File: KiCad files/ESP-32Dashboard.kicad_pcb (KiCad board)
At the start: 2 copper layers, 43.9 x 47 mm, 5 parts, among them J1 Conn_01x08_Pin, J4 JST-BEC, U1 XIAO-ESP32-S3-SMD

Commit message: Small changes to the pcb + new renders
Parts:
- moved J4 6.72 mm to (95.5, 98.6), turned to 0 degrees
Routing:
- net Net-(J4-Pin_1): track 63.3 -> 56.4 mm
- net GND: track 73.7 -> 76.5 mm

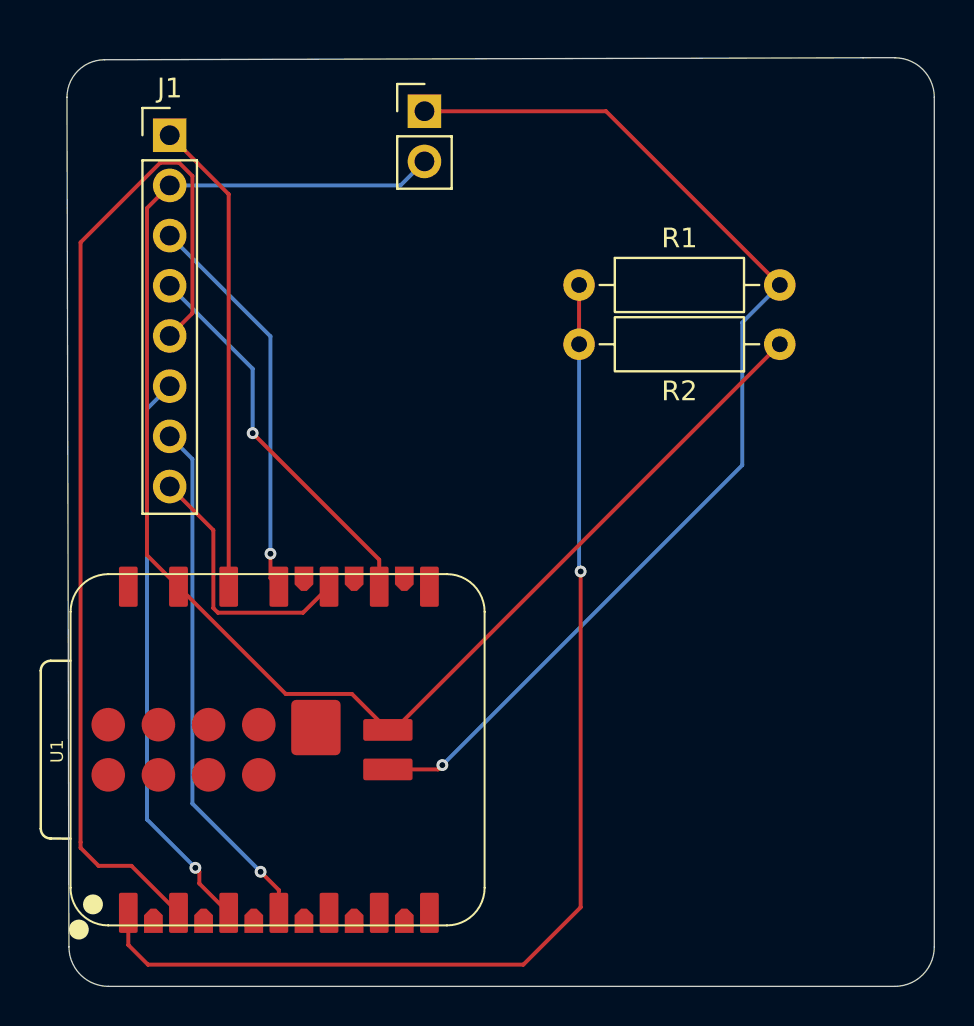
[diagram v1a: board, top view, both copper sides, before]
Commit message: fixed edge.cuts
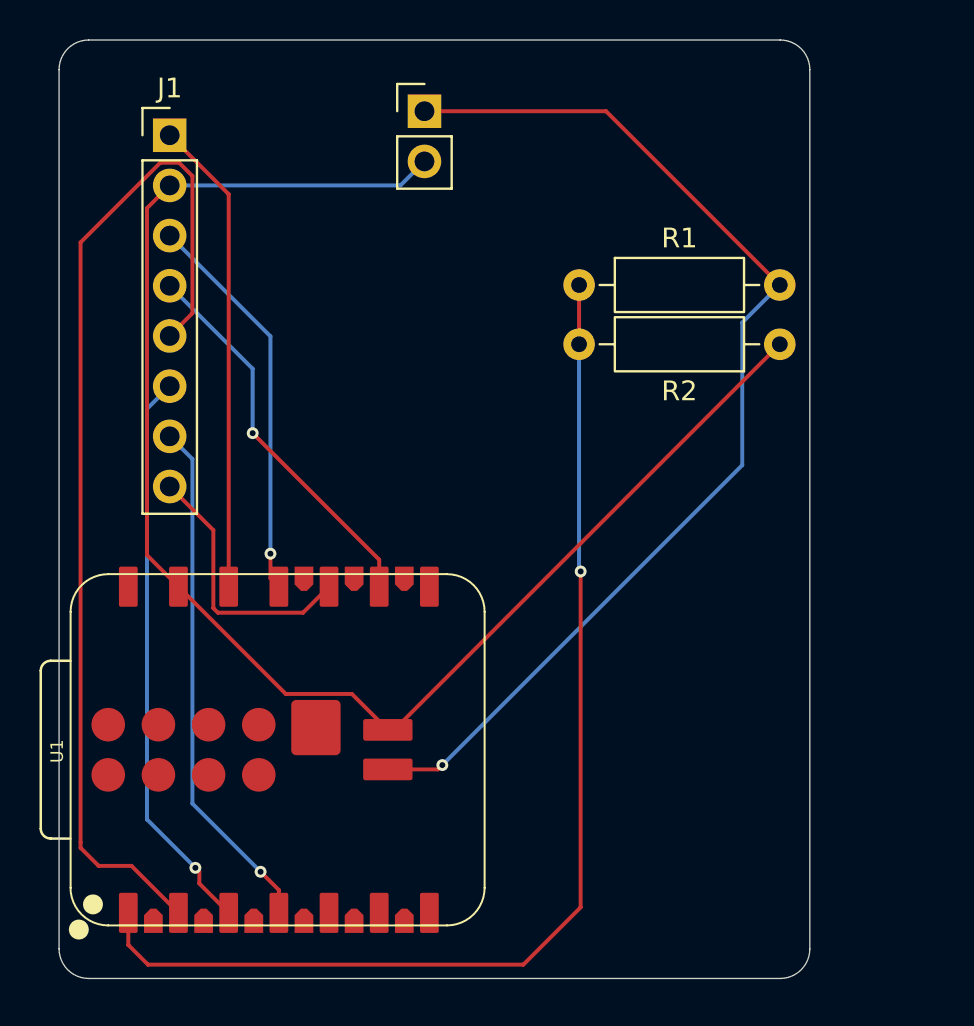
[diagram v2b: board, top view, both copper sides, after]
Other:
- board size 43.9 x 47 mm -> 38 x 47.5 mm
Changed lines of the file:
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@@
 	)
 	(gr_arc
-		(start 77.4 97.9)
-		(mid 77.956497 96.556497)
-		(end 79.3 96)
+		(start 77 96.5)
+		(mid 77.43934 95.43934)
+		(end 78.5 95)
 		(stroke
 			(width 0.05)
@@
 	)
 	(gr_line
-		(start 77.5 140.9)
-		(end 77.4 97.9)
+		(start 77 141)
+		(end 77 96.5)
 		(stroke
 			(width 0.05)
@@
 	)
 	(gr_line
-		(start 79.3 96)
-		(end 117.7 95.9)
+		(start 78.5 95)
+		(end 113.5 95)
 		(stroke
 			(width 0.05)
@@
 	)
 	(gr_arc
-		(start 79.5 142.9)
-		(mid 78.085786 142.314214)
-		(end 77.5 140.9)
+		(start 78.5 142.5)
+		(mid 77.43934 142.06066)
+		(end 77 141)
+		(stroke
+			(width 0.05)
+			(type default)
+		)
+		(layer "Edge.Cuts")
+	)
+	(gr_arc
+		(start 113.5 95)
+		(mid 114.56066 95.43934)
+		(end 115 96.5)
 		(stroke
 			(width 0.05)
@@
 	)
 	(gr_line
-		(start 117.7 95.9)
-		(end 119.3 95.895833)
+		(start 113.5 142.5)
+		(end 78.5 142.5)
+		(stroke
+			(width 0.05)
+			(type default)
+		)
+		(layer "Edge.Cuts")
+	)
+	(gr_line
+		(start 115 96.5)
+		(end 115 141)
 		(stroke
 			(width 0.05)
@@
 	)
 	(gr_arc
-		(start 119.3 95.9)
-		(mid 120.714214 96.485786)
-		(end 121.3 97.9)
-		(stroke
-			(width 0.05)
-			(type default)
-		)
-		(layer "Edge.Cuts")
-	)
-	(gr_line
-		(start 119.3 142.9)
-		(end 79.5 142.9)
-		(stroke
-			(width 0.05)
-			(type default)
-		)
-		(layer "Edge.Cuts")
-	)
-	(gr_line
-		(start 121.3 97.9)
-		(end 121.3 140.9)
-		(stroke
-			(width 0.05)
-			(type default)
-		)
-		(layer "Edge.Cuts")
-	)
-	(gr_arc
-		(start 121.3 140.9)
-		(mid 120.714214 142.314214)
-		(end 119.3 142.9)
-		(stroke
-			(width 0.05)
-			(type default)
-		)
-		(layer "Edge.Cuts")
+		(start 115 141)
+		(mid 114.56066 142.06066)
+		(end 113.5 142.5)
+		(stroke
+			(width 0.05)
+			(type default)
+		)
+		(layer "Edge.Cuts")
+	)
+	(segment
+		(start 113.84 107.76)
+		(end 113.48 107.4)
+		(width 0.2)
+		(layer "F.Cu")
+		(net "Net-(J4-Pin_1)")
+	)
+	(segment
+		(start 96.181012 131.918988)
+		(end 93.642823 131.918988)
+		(width 0.2)
+		(layer "F.Cu")
+		(net "Net-(J4-Pin_1)")
+	)
+	(segment
+		(start 96.4 131.7)
+		(end 96.181012 131.918988)
+		(width 0.2)
+		(layer "F.Cu")
+		(net "Net-(J4-Pin_1)")
+	)
+	(segment
+		(start 104.685 98.605)
+		(end 95.495 98.605)
+		(width 0.2)
+		(layer "F.Cu")
+		(net "Net-(J4-Pin_1)")
+	)
+	(segment
+		(start 113.48 107.4)
+		(end 104.685 98.605)
+		(width 0.2)
+		(layer "F.Cu")
+		(net "Net-(J4-Pin_1)")
+	)
+	(via
+		(at 96.4 131.7)
+		(size 0.6)
+		(drill 0.3)
+		(layers "F.Cu" "B.Cu")
+		(net "Net-(J4-Pin_1)")
+	)
+	(segment
+		(start 111.58 109.3)
+		(end 111.58 116.52)
+		(width 0.2)
+		(layer "B.Cu")
+		(net "Net-(J4-Pin_1)")
+	)
+	(segment
+		(start 111.58 116.52)
+		(end 96.4 131.7)
+		(width 0.2)
+		(layer "B.Cu")
+		(net "Net-(J4-Pin_1)")
+	)
+	(segment
+		(start 113.48 107.4)
+		(end 111.58 109.3)
+		(width 0.2)
+		(layer "B.Cu")
+		(net "Net-(J4-Pin_1)")
+	)
+	(segment
+		(start 93.961012 129.918988)
+		(end 93.642823 129.918988)
+		(width 0.2)
+		(layer "F.Cu")
+		(net "GND")
+	)
+	(segment
+		(start 83.045 122.67)
+		(end 88.475 128.1)
+		(width 0.2)
+		(layer "F.Cu")
+		(net "GND")
+	)
+	(segment
+		(start 88.475 128.1)
+		(end 91.823835 128.1)
+		(width 0.2)
+		(layer "F.Cu")
+		(net "GND")
+	)
+	(segment
+		(start 81.45 103.51)
+		(end 81.45 121.075)
+		(width 0.2)
+		(layer "F.Cu")
+		(net "GND")
+	)
+	(segment
+		(start 82.6 102.36)
+		(end 81.45 103.51)
+		(width 0.2)
+		(layer "F.Cu")
+		(net "GND")
+	)
+	(segment
+		(start 81.45 121.075)
+		(end 83.045 122.67)
+		(width 0.2)
+		(layer "F.Cu")
+		(net "GND")
+	)
+	(segment
+		(start 113.58 110.3)
+		(end 113.48 110.4)
+		(width 0.2)
+		(layer "F.Cu")
+		(net "GND")
+	)
+	(segment
+		(start 113.48 110.4)
+		(end 93.961012 129.918988)
+		(width 0.2)
+		(layer "F.Cu")
+		(net "GND")
+	)
+	(segment
+		(start 91.823835 128.1)
+		(end 93.642823 129.918988)
+		(width 0.2)
+		(layer "F.Cu")
+		(net "GND")
+	)
+	(segment
+		(start 94.28 102.36)
+		(end 95.495 101.145)
+		(width 0.2)
+		(layer "B.Cu")
+		(net "GND")
+	)
+	(segment
+		(start 82.6 102.36)
+		(end 94.28 102.36)
+		(width 0.2)
+		(layer "B.Cu")
+		(net "GND")
 	)
 	(segment
@@
 		(layer "B.Cu")
 		(net "Net-(U1-GPIO1_A0_D0)")
-	)
-	(segment
-		(start 113.84 107.76)
-		(end 113.48 107.4)
-		(width 0.2)
-		(layer "F.Cu")
-		(net "Net-(J4-Pin_1)")
-	)
-	(segment
-		(start 96.181012 131.918988)
-		(end 93.642823 131.918988)
-		(width 0.2)
-		(layer "F.Cu")
-		(net "Net-(J4-Pin_1)")
-	)
-	(segment
-		(start 96.4 131.7)
-		(end 96.181012 131.918988)
-		(width 0.2)
-		(layer "F.Cu")
-		(net "Net-(J4-Pin_1)")
-	)
-	(segment
-		(start 104.685 98.605)
-		(end 95.495 98.605)
-		(width 0.2)
-		(layer "F.Cu")
-		(net "Net-(J4-Pin_1)")
-	)
-	(segment
-		(start 113.48 107.4)
-		(end 104.685 98.605)
-		(width 0.2)
-		(layer "F.Cu")
-		(net "Net-(J4-Pin_1)")
-	)
-	(via
-		(at 96.4 131.7)
-		(size 0.6)
-		(drill 0.3)
-		(layers "F.Cu" "B.Cu")
-		(net "Net-(J4-Pin_1)")
-	)
-	(segment
-		(start 111.58 109.3)
-		(end 111.58 116.52)
-		(width 0.2)
-		(layer "B.Cu")
-		(net "Net-(J4-Pin_1)")
-	)
-	(segment
-		(start 111.58 116.52)
-		(end 96.4 131.7)
-		(width 0.2)
-		(layer "B.Cu")
-		(net "Net-(J4-Pin_1)")
-	)
-	(segment
-		(start 113.48 107.4)
-		(end 111.58 109.3)
-		(width 0.2)
-		(layer "B.Cu")
-		(net "Net-(J4-Pin_1)")
 	)
 	(segment
@@
 		(net "+3V3")
 	)
-	(segment
-		(start 93.961012 129.918988)
-		(end 93.642823 129.918988)
-		(width 0.2)
-		(layer "F.Cu")
-		(net "GND")
-	)
-	(segment
-		(start 83.045 122.67)
-		(end 88.475 128.1)
-		(width 0.2)
-		(layer "F.Cu")
-		(net "GND")
-	)
-	(segment
-		(start 88.475 128.1)
-		(end 91.823835 128.1)
-		(width 0.2)
-		(layer "F.Cu")
-		(net "GND")
-	)
-	(segment
-		(start 81.45 103.51)
-		(end 81.45 121.075)
-		(width 0.2)
-		(layer "F.Cu")
-		(net "GND")
-	)
-	(segment
-		(start 82.6 102.36)
-		(end 81.45 103.51)
-		(width 0.2)
-		(layer "F.Cu")
-		(net "GND")
-	)
-	(segment
-		(start 81.45 121.075)
-		(end 83.045 122.67)
-		(width 0.2)
-		(layer "F.Cu")
-		(net "GND")
-	)
-	(segment
-		(start 113.58 110.3)
-		(end 113.48 110.4)
-		(width 0.2)
-		(layer "F.Cu")
-		(net "GND")
-	)
-	(segment
-		(start 113.48 110.4)
-		(end 93.961012 129.918988)
-		(width 0.2)
-		(layer "F.Cu")
-		(net "GND")
-	)
-	(segment
-		(start 91.823835 128.1)
-		(end 93.642823 129.918988)
-		(width 0.2)
-		(layer "F.Cu")
-		(net "GND")
-	)
-	(segment
-		(start 94.28 102.36)
-		(end 95.495 101.145)
-		(width 0.2)
-		(layer "B.Cu")
-		(net "GND")
-	)
-	(segment
-		(start 82.6 102.36)
-		(end 94.28 102.36)
-		(width 0.2)
-		(layer "B.Cu")
-		(net "GND")
-	)
 	(embedded_fonts no)
